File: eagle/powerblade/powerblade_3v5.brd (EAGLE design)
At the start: 25.4 x 25.4 mm, 78 parts, among them J1 JTAG_14PIN_IDC-ND, J2 AC_IN51, J4 TC2030-JLINK-NL, Q1 NTS4173, Q4 2SK1829, U1 TPS62122, U2 MCP6V3, U3 MSP430FR5738, U4 NRF51822QF, U6 MAX9910, U7 OPA2369, X1 16MHz, X3 32.768kHz, Y1 UREACH_XTEND

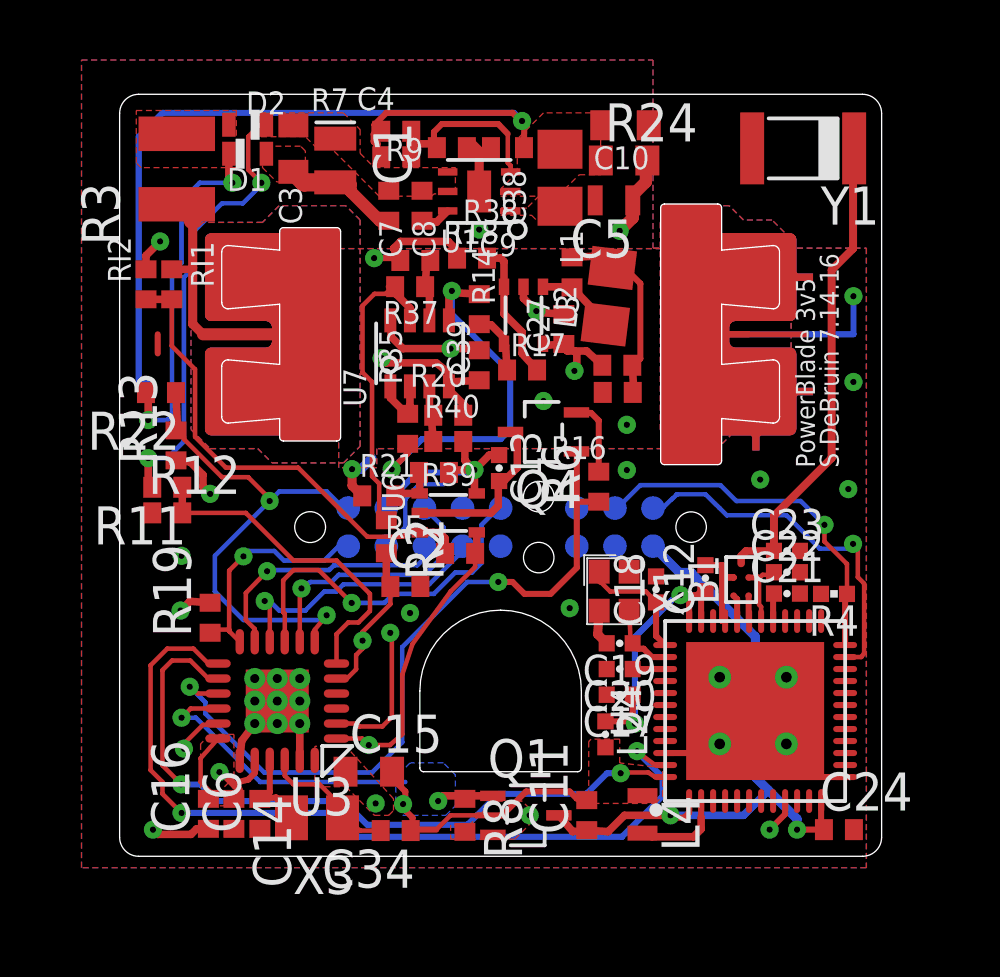
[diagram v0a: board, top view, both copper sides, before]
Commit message: removed random trace on bottom of board
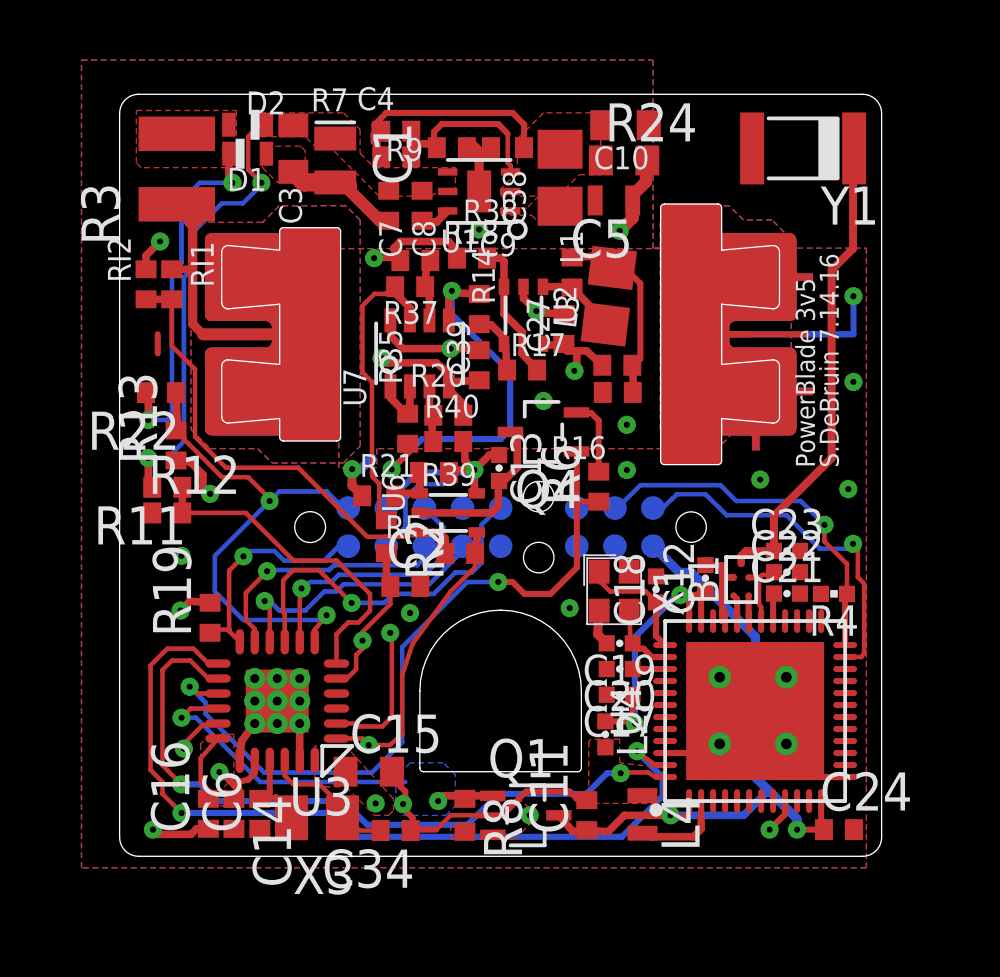
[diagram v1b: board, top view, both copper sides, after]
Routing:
- net VS+: track 29.5 -> 7.74 mm, vias 1 -> 0
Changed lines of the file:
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@@
 <?xml version="1.0" encoding="utf-8"?>
 <!DOCTYPE eagle SYSTEM "eagle.dtd">
-<eagle version="6.5.0">
+<eagle version="6.3">
 <drawing>
 <settings>
@@
 <contactref element="R24" pad="1"/>
 <wire x1="0.7786" y1="6.223" x2="0.788125" y2="6.990625" width="0.2032" layer="1"/>
-<wire x1="0.714375" y1="7.064375" x2="0.396875" y2="7.381875" width="0.2032" layer="1"/>
+<wire x1="0.788125" y1="6.990625" x2="0.396875" y2="7.381875" width="0.2032" layer="1"/>
 <wire x1="0.396875" y1="7.381875" x2="-3.81" y2="7.381875" width="0.2032" layer="1"/>
 <wire x1="-3.81" y1="7.381875" x2="-4.206875" y2="6.985" width="0.2032" layer="1"/>
@@
 <wire x1="-4.1275" y1="5.8" x2="-3.9798" y2="5.9182" width="0.254" layer="1"/>
 <wire x1="-3.9798" y1="6.7691" x2="-4.206875" y2="6.6675" width="0.254" layer="1"/>
-<via x="0.714375" y="7.112" extent="1-16" drill="0.2032"/>
-<wire x1="0.788125" y1="6.990625" x2="0.714375" y2="7.064375" width="0.2032" layer="1"/>
-<wire x1="0.714375" y1="7.064375" x2="0.714375" y2="7.112" width="0.2032" layer="1"/>
 <polygon width="0.2032" layer="1" thermals="no" rank="2">
 <vertex x="0" y="4.60375"/>
@@
 <vertex x="0" y="4.841875"/>
 </polygon>
-<wire x1="0.714375" y1="7.112" x2="0.4445" y2="7.381875" width="0.2032" layer="16"/>
-<wire x1="0.4445" y1="7.381875" x2="-11.27125" y2="7.381875" width="0.2032" layer="16"/>
-<wire x1="-11.27125" y1="7.381875" x2="-12.065" y2="6.588125" width="0.2032" layer="16"/>
-<wire x1="-12.065" y1="6.588125" x2="-12.065" y2="-1.508125" width="0.2032" layer="16"/>
-<wire x1="-12.065" y1="-1.508125" x2="-11.668125" y2="-1.666875" width="0.2032" layer="16"/>
 </signal>
 <signal name="N$10">
